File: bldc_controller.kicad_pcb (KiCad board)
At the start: 4 copper layers, 99.1 x 99.1 mm, 144 parts, among them J1 Conn_01x06_Male, J2 Banana_Jack, J3 Banana_Jack, Q1 2N7002E, Q10 IRLB8721PBF, Q11 IRLB8721PBF, Q2 DMN65D8L-7, Q3 DMN65D8L-7, Q4 MMBT3904, Q5 IRF4905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

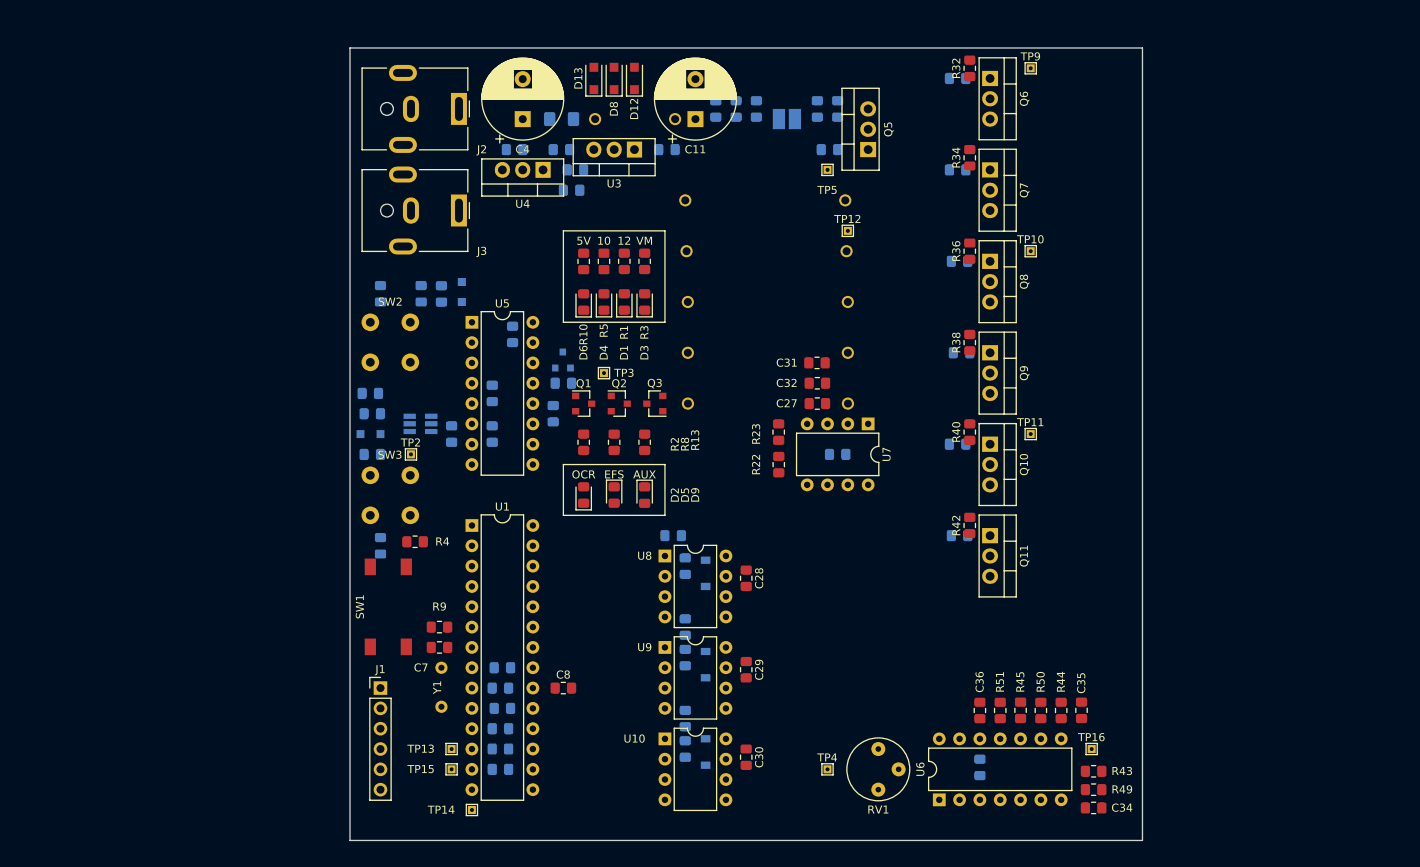
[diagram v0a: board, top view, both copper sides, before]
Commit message: Done with First Pass of Layout
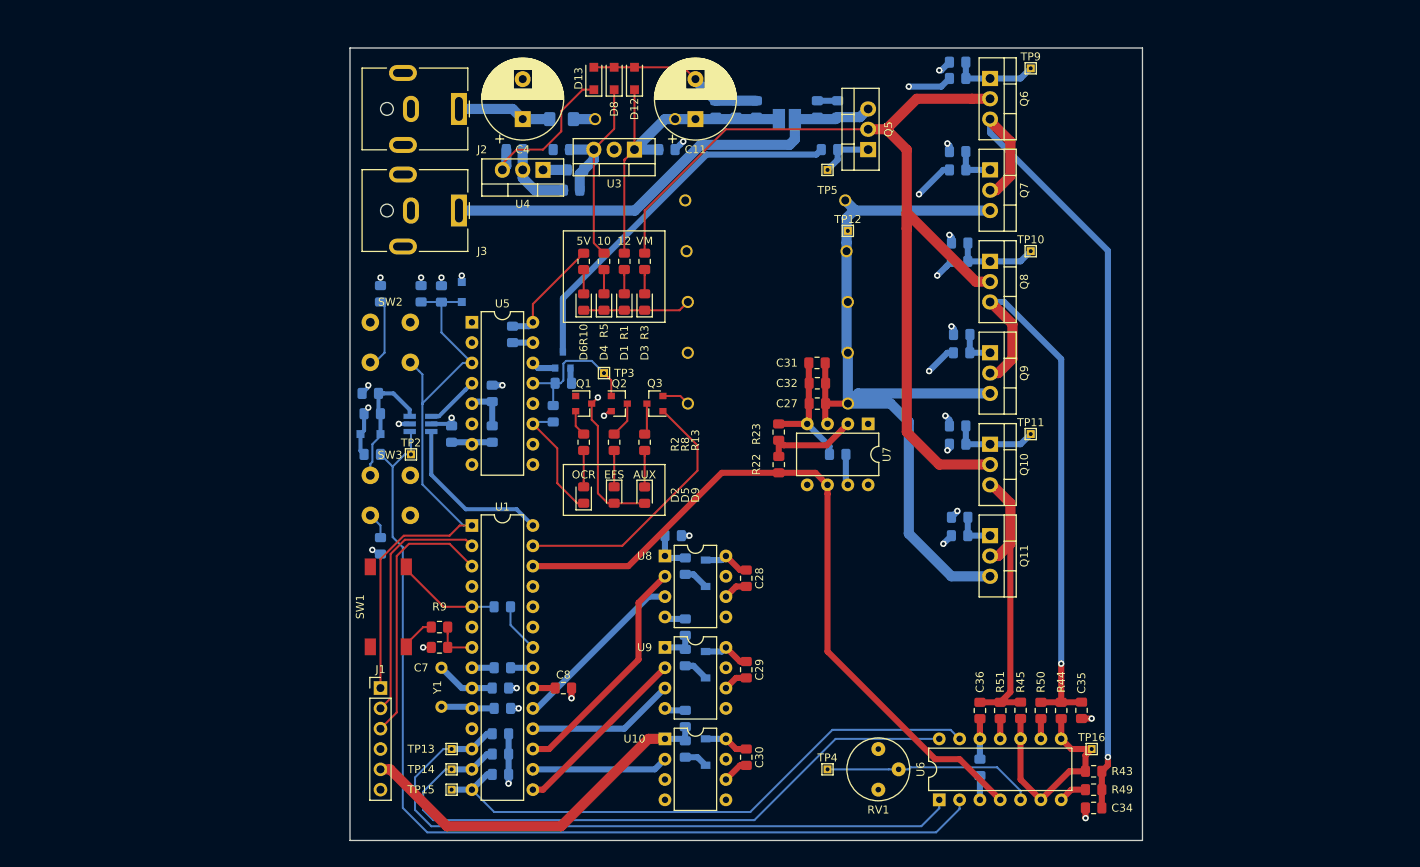
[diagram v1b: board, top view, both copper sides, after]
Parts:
- R32, R34, R36, R38, R4, R40, R42: moved to B.Cu
- moved R4 13.6 mm to (119.4, 110.5), turned to 0 degrees
- moved TP14 5.68 mm to (113.0, 130.8)
- moved R48 3.17 mm to (119.1, 131.4)
- moved TP15 2.54 mm to (113.0, 133.3)
- moved R47 1.91 mm to (119.1, 128.9)
- moved R34 1.70 mm to (176.3, 53.6), turned to 180 degrees
- moved R40 1.70 mm to (176.3, 87.9), turned to 180 degrees
- moved R32 1.70 mm to (176.3, 42.4), turned to 180 degrees
- moved R42 1.63 mm to (176.5, 99.3), turned to 180 degrees
- moved R36 1.62 mm to (176.5, 65.0), turned to 180 degrees
- moved R38 1.43 mm to (176.8, 76.5), turned to 180 degrees
- moved R46 0.63 mm to (119.1, 126.4)
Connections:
- U1 pad 13: /BEMF_C -> /BEMF_B
- U1 pad 14: /BEMF_B -> /BEMF_C
- U1 pad 15: /MCU_A_SIG -> /MCU_B_SIG
- U1 pad 17: /MCU_B_SIG -> /MCU_A_SIG
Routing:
- net PhaseA: track 0.00 -> 190.0 mm, vias 0 -> 1
- net +10V: track 0.00 -> 174.8 mm
- net PhaseB: track 0.00 -> 139.6 mm, vias 0 -> 1
- net GNDD: track 0.00 -> 134.5 mm, vias 0 -> 20
- net /nI_ERR: track 0.00 -> 124.4 mm
- net VBUS: track 0.00 -> 121.3 mm
- net /I_RAW: track 0.00 -> 107.1 mm
- net PhaseC: track 0.00 -> 92.9 mm
- net /I_SENSE: track 0.00 -> 92.4 mm
- net +5V: track 0.00 -> 87.9 mm, vias 0 -> 7
- net /BEMF_A: track 0.00 -> 84.3 mm
- net Net-(R31-Pad2): track 0.00 -> 82.6 mm, vias 0 -> 1
- net /BEMF_B: track 0.00 -> 82.1 mm
- net /nRESET: track 0.00 -> 76.2 mm
- net /BEMF_C: track 0.00 -> 72.7 mm
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- added copper zone on In1.Cu, net +5V
- added copper zone on In2.Cu, net GNDD

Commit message: Forgot a Connection
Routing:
- net GNDD: track 134.5 -> 138.3 mm
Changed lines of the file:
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@@
     (thickness 1.6)
     (drawings 19)
-    (tracks 607)
+    (tracks 608)
     (zones 0)
     (modules 144)
@@
   (page A4)
   (layers
-    (0 F.Cu signal)
+    (0 F.Cu signal hide)
     (1 In1.Cu power hide)
-    (2 In2.Cu power hide)
+    (2 In2.Cu power)
     (31 B.Cu signal)
     (32 B.Adhes user)
@@
   )
   (setup
-    (last_trace_width 0.254)
+    (last_trace_width 1.27)
     (user_trace_width 0.254)
     (user_trace_width 0.508)
@@
   (via (at 142.748 101.6) (size 0.8) (drill 0.4) (layers F.Cu B.Cu) (net 1))
   (segment (start 141.75 101.6) (end 142.748 101.6) (width 0.762) (layer B.Cu) (net 1))
+  (segment (start 121.92 53.34) (end 125.73 53.34) (width 1.27) (layer B.Cu) (net 1))
   (segment (start 108.969999 81.029999) (end 107.87 79.93) (width 0.254) (layer B.Cu) (net 2))
   (segment (start 109.382999 81.442999) (end 108.969999 81.029999) (width 0.254) (layer B.Cu) (net 2))

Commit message: Added some shapes
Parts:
- removed J3: Banana_Jack, Connector_BarrelJack:BarrelJack_CUI_PJ-063AH_Horizontal
- added FB2: BL01RN1A1D2B, Ferrite_THT:Ferrite_Bead_TH, F.Cu at (64.3, 52.1)
- added TP6: TestPoint, TestPoint:TestPoint_THTPad_1.0x1.0mm_Drill0.5mm, F.Cu at (63.9, 39.1)
- added TP7: TestPoint, TestPoint:TestPoint_THTPad_1.0x1.0mm_Drill0.5mm, F.Cu at (67.0, 39.1)
- added TP8: TestPoint, TestPoint:TestPoint_THTPad_1.0x1.0mm_Drill0.5mm, F.Cu at (70.0, 39.1)
- C15, C17, C20, C21, F1, JP1, R18, R20: moved to F.Cu
- J2: value Banana_Jack -> Screw_Terminal_01x04; footprint Connector_BarrelJack:BarrelJack_CUI_PJ-063AH_Horizontal -> Connector:Terminal_Block_4Pin_TH
- moved D12 31.3 mm to (117.6, 69.8), turned to 270 degrees
- moved D8 28.6 mm to (120.1, 69.8), turned to 270 degrees
- moved D13 26.7 mm to (122.7, 69.8), turned to 270 degrees
- moved J2 13.3 mm to (105.7, 58.6)
- moved R14 10.3 mm to (122.9, 64.5)
- moved U4 10.2 mm to (119.1, 64.5)
- moved C14 10.2 mm to (115.6, 62.0)
- moved C13 9.54 mm to (122.7, 62.0)
- moved C5 9.54 mm to (135.9, 62.0)
- moved U3 9.54 mm to (131.8, 62.0)
- moved C6 6.10 mm to (128.0, 64.5), turned to 0 degrees
- moved C4 5.93 mm to (116.1, 50.5)
- moved R18 5.34 mm to (159.0, 53.6), turned to 270 degrees
- moved C21 5.33 mm to (161.3, 53.6), turned to 270 degrees
- moved TP16 5.21 mm to (196.8, 124.7)
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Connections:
- C11 pad 2: GNDD -> GNDPWR
- C15 pad 2: GNDD -> GNDPWR
- C17 pad 2: GNDD -> GNDPWR
- C20 pad 2: GNDD -> GNDPWR
- C4 pad 2: GNDD -> GNDPWR
- J2 pad 2: GNDD -> Vdrive
- R21 pad 2: GNDD -> GNDPWR
- R24 pad 2: GNDD -> GNDPWR
- R25 pad 2: GNDD -> GNDPWR
- R29 pad 2: GNDD -> GNDPWR
- R30 pad 2: GNDD -> GNDPWR
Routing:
- net PhaseA: track 190.0 -> 95.7 mm, vias 1 -> 22
- net VBUS: track 121.3 -> 58.3 mm
- net PhaseB: track 139.6 -> 87.2 mm
- net Vdrive: track 57.9 -> 6.68 mm
- net GNDD: track 138.3 -> 90.0 mm, vias 20 -> 24
- net Net-(Q4-Pad3): track 46.7 -> 6.70 mm
- net +10V: track 174.8 -> 141.4 mm
- net +12V: track 43.6 -> 11.8 mm
- net +5V: track 87.9 -> 62.2 mm
- net PhaseC: track 92.9 -> 71.8 mm
- net /nRESET: track 76.2 -> 60.0 mm
- net +BATT: track 11.9 -> 0.00 mm
- net /NEUTRAL: track 28.2 -> 20.6 mm
- net Net-(Q6-Pad1): track 10.7 -> 7.11 mm
- net Net-(R49-Pad2): track 3.56 -> 0.00 mm
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- added copper zone on F.Cu, net +12V
- added copper zone on F.Cu, net +BATT
- added copper zone on F.Cu, net Net-(F1-Pad1)
- added copper zone on B.Cu, net PhaseA
- added copper zone on F.Cu, net PhaseA
- added copper zone on B.Cu, net PhaseB
- added copper zone on F.Cu, net PhaseB
- added copper zone on B.Cu, net PhaseC
- added copper zone on F.Cu, net PhaseC
- added copper zone on F.Cu, net VBUS
- added copper zone on F.Cu, net Vdrive
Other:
- outline, holes or cut-outs redrawn

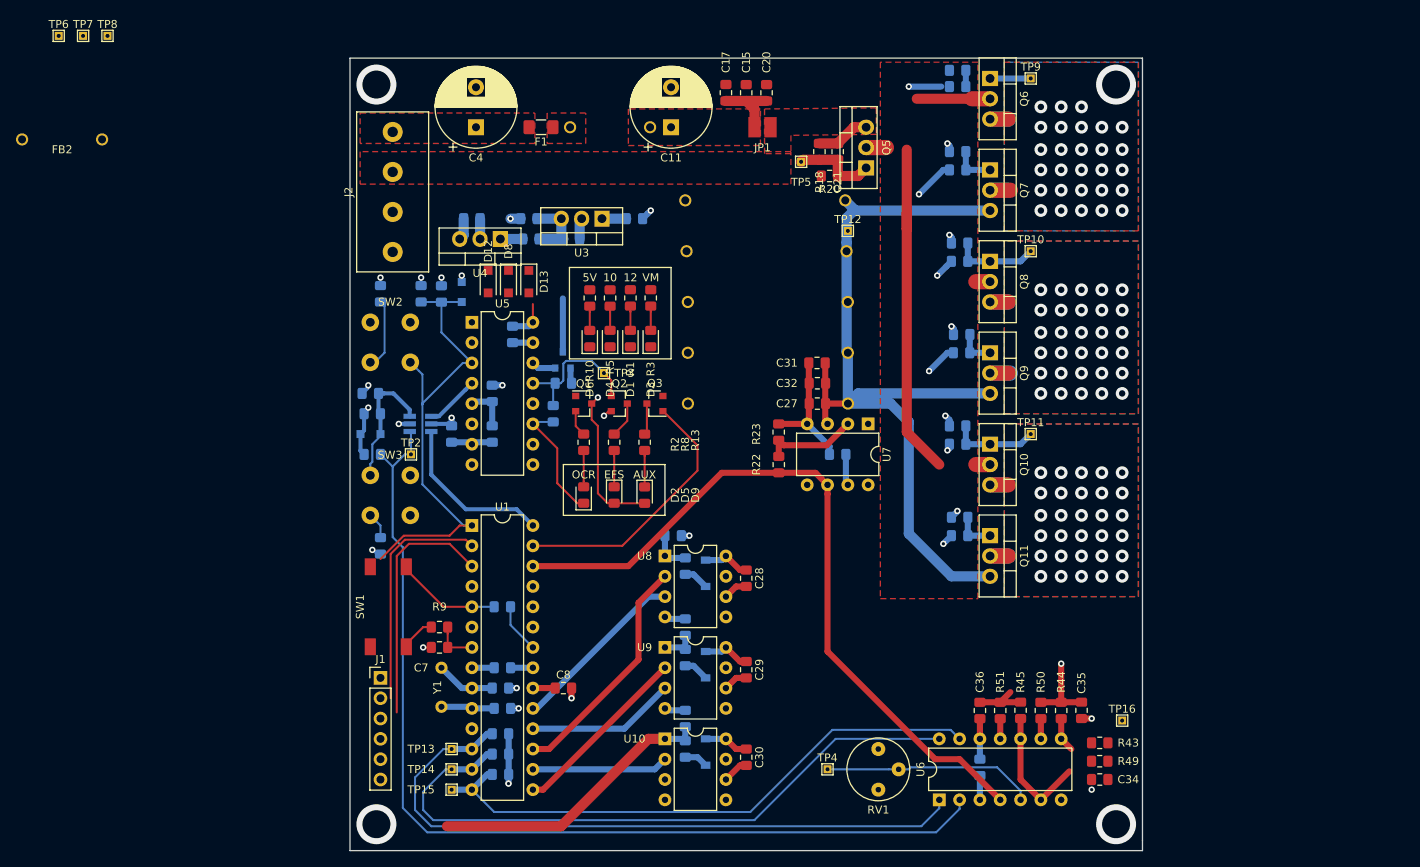
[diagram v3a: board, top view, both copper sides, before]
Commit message: Finished Ground Planes
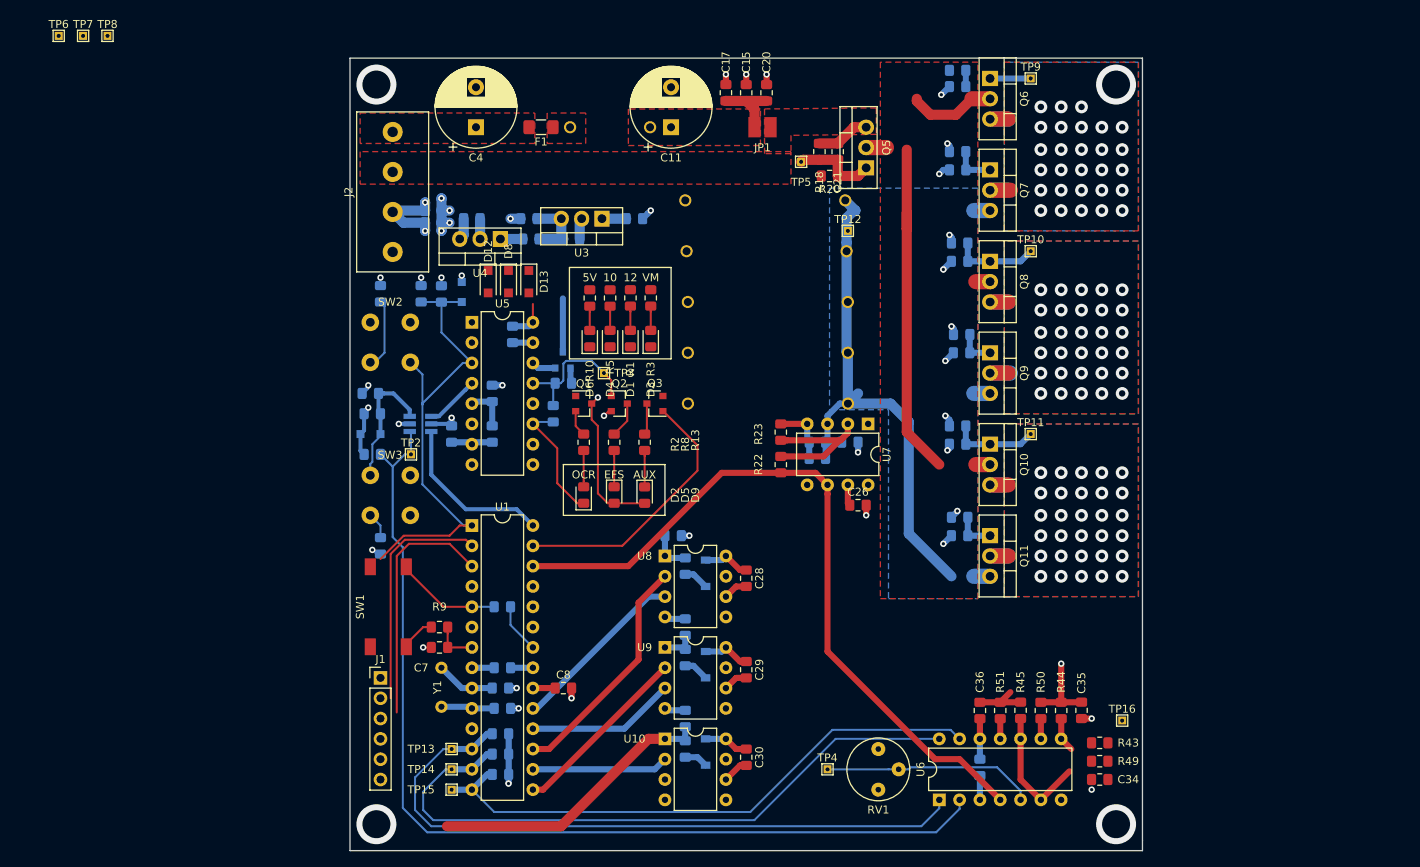
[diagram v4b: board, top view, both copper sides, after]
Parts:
- removed FB2: BL01RN1A1D2B, Ferrite_THT:Ferrite_Bead_TH
- added R52: 0, Resistor_SMD:R_0805_2012Metric_Pad1.15x1.40mm_HandSolder, B.Cu at (110.7, 62.5)
- added R53: 0, Resistor_SMD:R_0805_2012Metric_Pad1.15x1.40mm_HandSolder, B.Cu at (110.7, 61.0)
- C26: moved to F.Cu
- C27, C31, C32: moved to B.Cu
- moved C31 10.7 mm to (162.8, 89.9), turned to 0 degrees
- moved C32 9.40 mm to (158.8, 91.9)
- moved C26 6.84 mm to (163.8, 97.8), turned to 0 degrees
- moved C27 4.83 mm to (158.8, 89.9)
- moved R23 0.26 mm to (154.2, 88.7)
- moved R22 0.25 mm to (154.2, 92.7)
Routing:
- net /I_RAW: track 107.1 -> 75.1 mm
- net GNDPWR: track 0.00 -> 14.6 mm, vias 0 -> 5
- net Net-(R22-Pad2): track 12.0 -> 18.2 mm
- net Net-(R31-Pad2): track 81.1 -> 79.2 mm
- net VBUS: track 58.3 -> 60.1 mm
- net +5V: track 62.2 -> 61.3 mm
- net GNDD: track 90.0 -> 90.4 mm, vias 24 -> 26
- net PhaseC: vias 0 -> 30
- net PhaseB: vias 1 -> 31
- net PhaseA: vias 22 -> 28
- net (no net): vias 66 -> 4
- added copper zone on B.Cu, net /I_RAW
- added copper zone on In2.Cu, net GNDPWR

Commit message: Almost Done with Layout V2
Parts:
- added C10: 1uF, Capacitor_SMD:C_0805_2012Metric_Pad1.15x1.40mm_HandSolder, F.Cu at (155.7, 46.2)
- added C37: 0.1uF, Capacitor_SMD:C_0805_2012Metric_Pad1.15x1.40mm_HandSolder, F.Cu at (161.3, 46.2)
- added C9: 22uF, Capacitor_SMD:C_0805_2012Metric_Pad1.15x1.40mm_HandSolder, F.Cu at (158.5, 46.2)
- R21, R24, R25, R29, R30: moved to F.Cu
- moved TP8 129.7 mm to (189.2, 90.2)
- moved TP7 125.5 mm to (189.2, 67.3)
- moved TP6 125.4 mm to (189.2, 44.5)
- moved TP4 67.5 mm to (227.1, 122.9)
- moved RV1 65.6 mm to (228.1, 105.9)
- moved TP16 17.6 mm to (186.4, 138.9)
- moved C23 14.7 mm to (155.5, 102.1)
- moved C24 14.7 mm to (157.0, 113.5)
- moved C25 14.7 mm to (157.0, 125.0)
- moved C28 14.7 mm to (164.6, 107.4)
- moved C29 14.7 mm to (164.6, 118.9)
- moved C30 14.7 mm to (164.6, 129.8)
- moved D14 14.7 mm to (159.5, 106.8)
- moved D15 14.7 mm to (159.5, 118.2)
- moved R26 14.7 mm to (157.0, 105.9)
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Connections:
- U1 pad 13: /BEMF_B -> /BEMF_C
- U1 pad 14: /BEMF_C -> /BEMF_B
- U1 pad 15: /MCU_B_SIG -> /MCU_C_SIG
- U1 pad 16: /MCU_C_SIG -> /MCU_B_SIG
- U1 pad 18: /MCU_B_EN -> /MCU_C_EN
- U1 pad 19: /MCU_A_EN -> /MCU_B_EN
- U1 pad 23: /MCU_C_EN -> /MCU_A_EN
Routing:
- net +10V: track 141.4 -> 88.5 mm, vias 0 -> 2
- net PhaseA: track 95.7 -> 138.0 mm, vias 28 -> 29
- net Net-(Q4-Pad3): track 6.70 -> 45.5 mm, vias 0 -> 1
- net VBUS: track 60.1 -> 96.5 mm, vias 0 -> 1
- net +5V: track 61.3 -> 92.5 mm
- net Net-(RV1-Pad2): track 26.6 -> 0.00 mm
- net +12V: track 11.8 -> 34.5 mm
- net /I_SENSE: track 92.4 -> 111.6 mm
- net GNDD: track 90.4 -> 107.6 mm, vias 26 -> 34
- net /nRESET: track 60.0 -> 76.1 mm
- net /MCU_C_SIG: track 17.0 -> 32.6 mm
- net /MCU_B_EN: track 18.6 -> 32.6 mm
- net /MCU_B_SIG: track 22.8 -> 36.3 mm
- net /BEMF_C: track 72.7 -> 84.9 mm
- net Net-(R31-Pad2): track 79.2 -> 67.2 mm
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- added copper zone on In1.Cu, net +10V
- added copper zone on B.Cu, net +12V
